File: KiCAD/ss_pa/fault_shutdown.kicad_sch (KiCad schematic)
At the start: 39 parts, among them J31 8P8C_Shielded, J5 Screw_Terminal_01x02, U1 LM393, U2 CD74HC4066, U3 LM2936-5.0_TO92

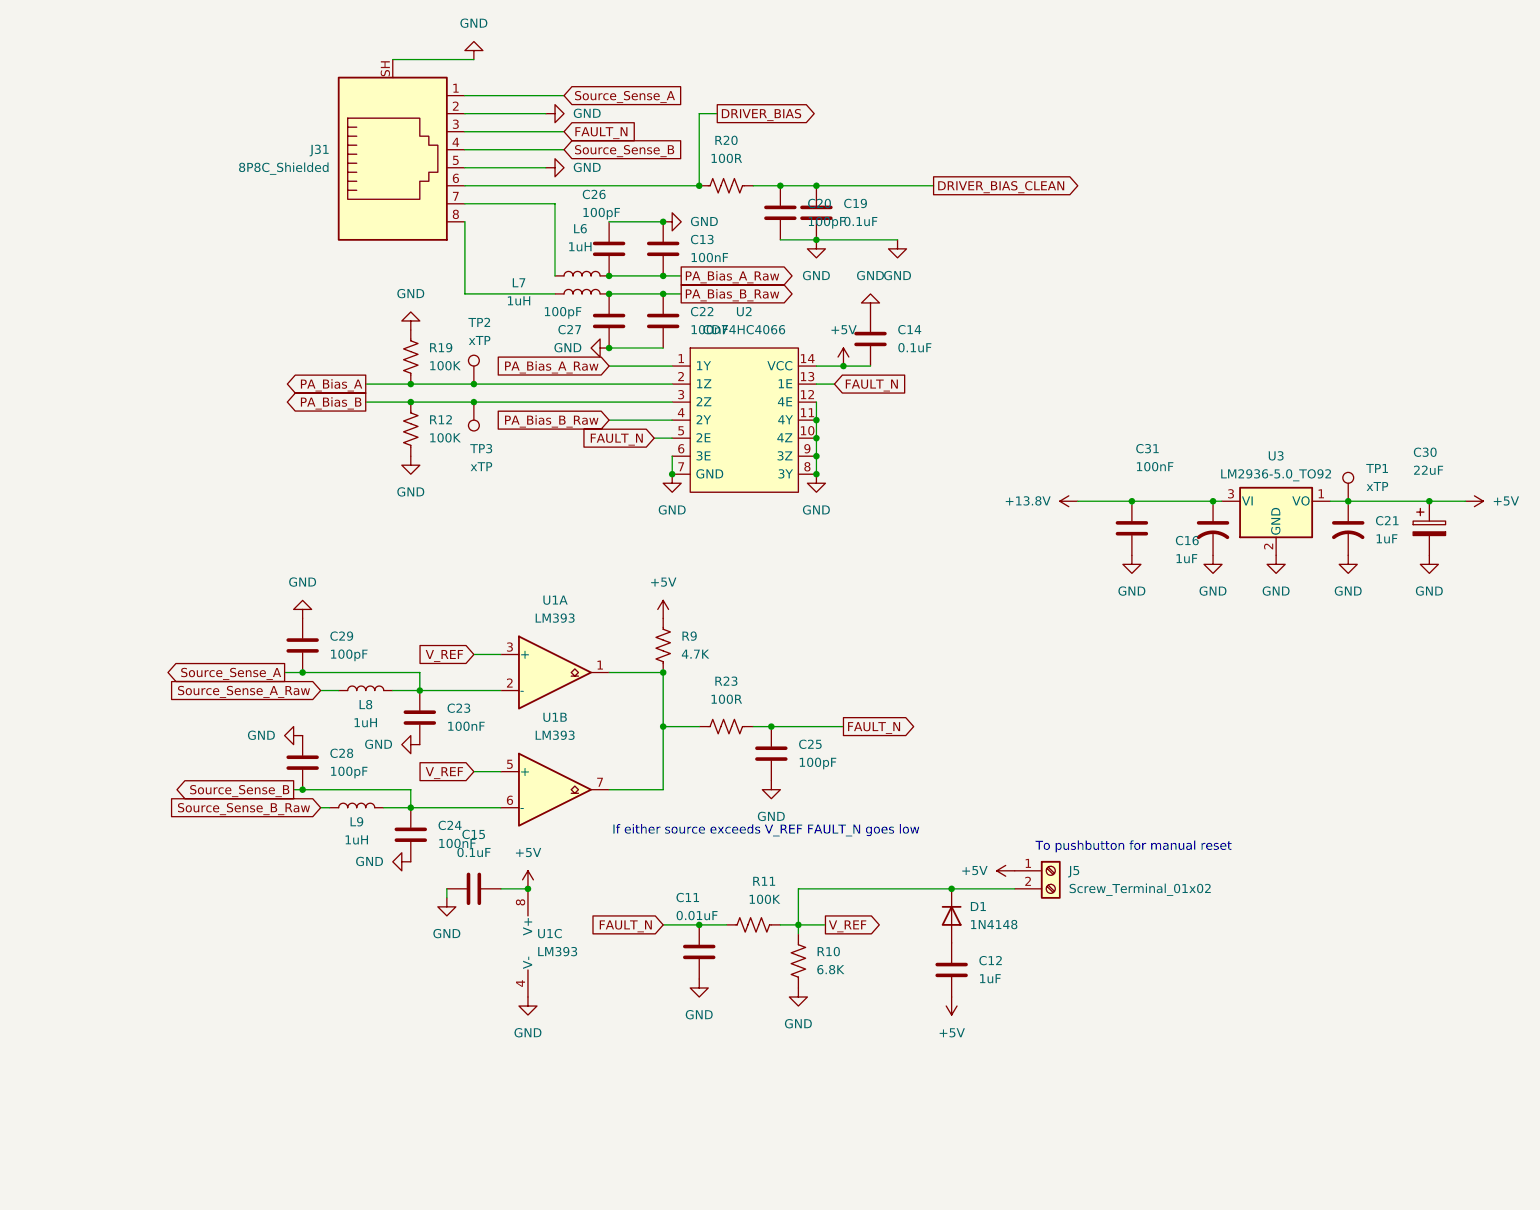
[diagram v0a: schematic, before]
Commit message: revD: ss_pa U13 LM2936 pinout fix + analog U9 74HCT125 miswiring fix
ss_pa fault_shutdown.kicad_sch: fix U13 pin-to-signal mapping so an
LM2936Z-5.0/NOPB can be installed without destruction (prior MCP1700
symbol had pin 1=GND, 2=VI, 3=VO; LM2936 datasheet is pin 1=VO, 2=GND,
3=VI).

analog dac.kicad_sch: fix U9 74HCT125 miswiring found during follow-up
audit.

Co-Authored-By: Claude Opus 4.7 <noreply@anthropic.com>
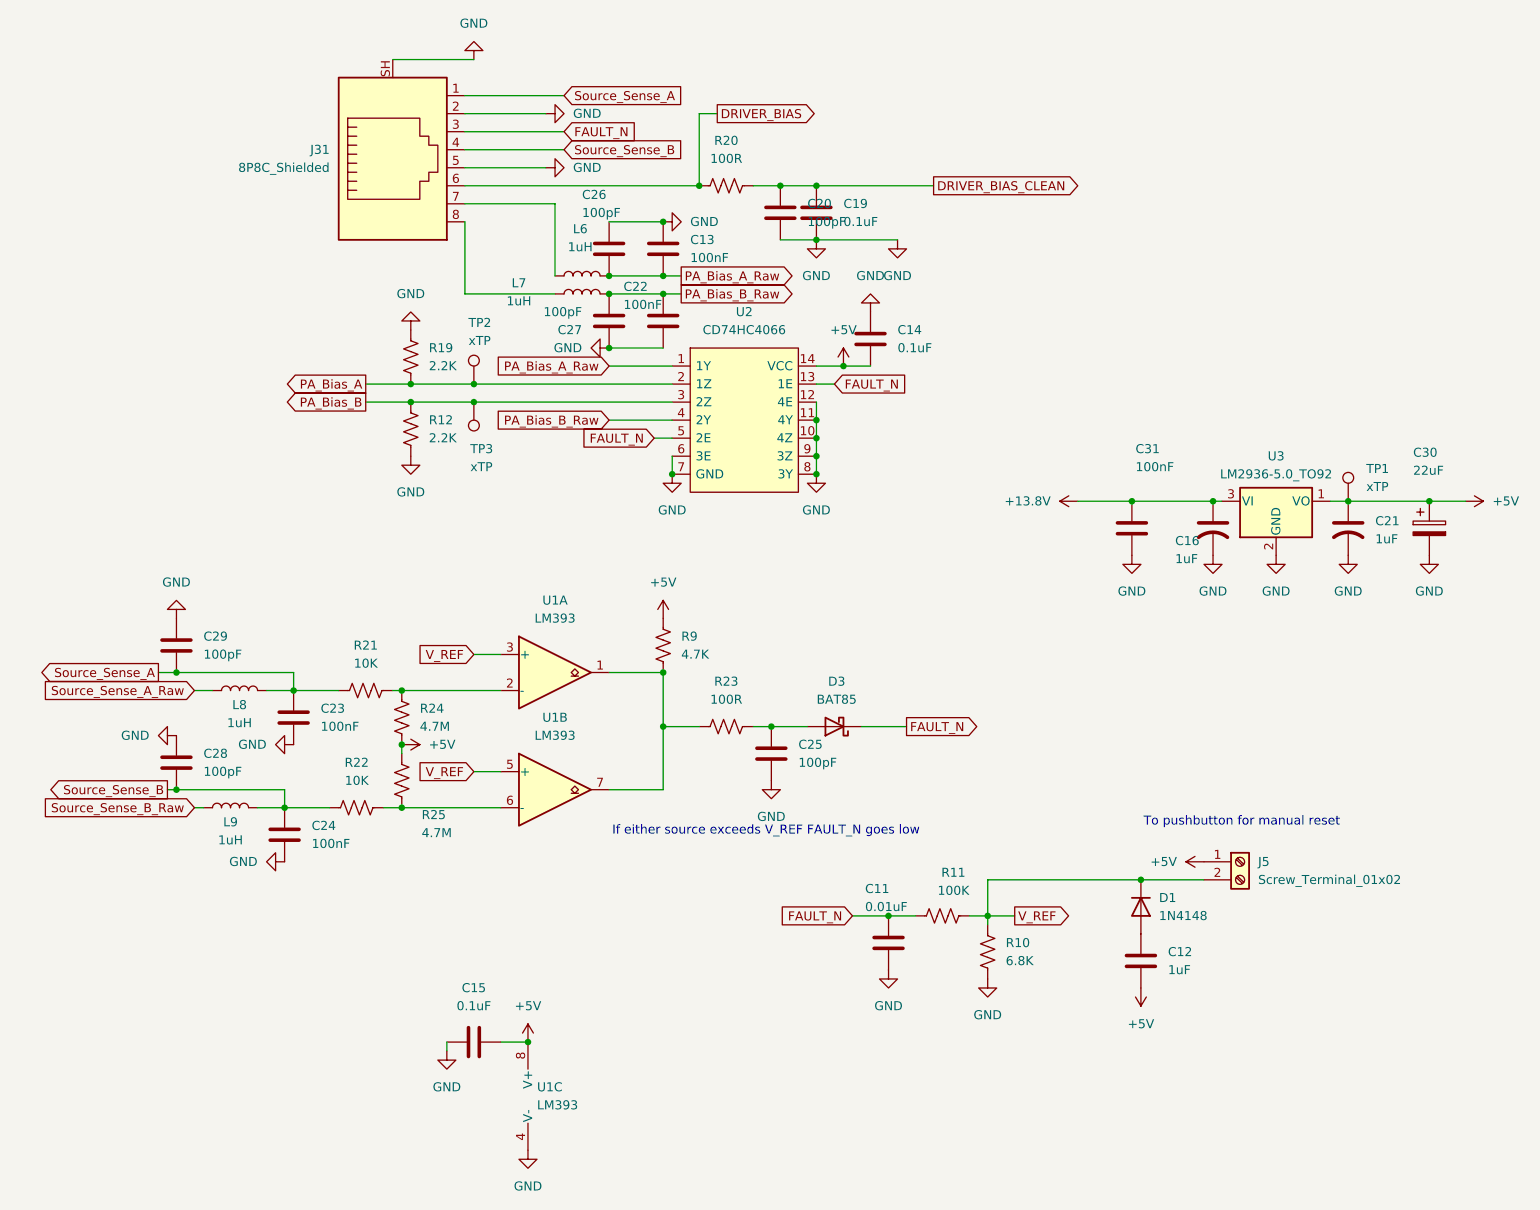
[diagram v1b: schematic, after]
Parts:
- added D3: BAT85, Diode_THT:D_DO-35_SOD27_P7.62mm_Horizontal, symbol Diode:BAT85
- added R21, R22: 10K, symbol Device:R_US
- added R24, R25: 4.7M, symbol Device:R_US
- R12, R19: value 100K -> 2.2K
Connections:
- net +5V: now also R24.2, R25.1
- net FAULT_N: now also D3.1 (K); no longer C25.1, R23.2
- net Source_Sense_A: now also R21.1; no longer U1.2 (-)
- net Source_Sense_B: now also R22.1; no longer U1.6 (-)
- new net: R22.2, R25.2, U1.6 (-)
- new net: C25.1, D3.2 (A), R23.2
- new net: R21.2, R24.1, U1.2 (-)
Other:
- moved on the sheet: C11, C12, C15, C23, C24, C28, C29, D1, J5, L8, L9, R10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

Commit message: revD: footprint pass across all boards + ss_pa fault-chain fix + LLM review brief
- New tools/assign_misc_footprints.py: lib_id-keyed footprint assigner
  (resistors, screw terminals, pin headers, LT1054); mirrors cap-script
  safe-write (UTF-8 no BOM, no CRLF translation).
- tools/assign_cap_footprints.py: added 0.47uF -> C_Rect_L7.0mm case.
- Ran both scripts across analog, ss_pa, Output LPF, frontpanel,
  protoshield, and shelved power board. ~100 fills; details in diffs.
- ss_pa: R1-R4 (0.22 ohm source sense) upgraded to 2W Yageo RSF200
  with DIN0516 L15.5mm/P20.32mm footprint; Value tagged "0.22R 2W".
  R15/R16 confirmed 1/4W (DIN0207) for BS170 source degeneration.
- analog/power: R44 15R 5W horizontal, P30.48mm footprint.
- ss_pa fault chain (from external LLM review): R21/R22 raised
  10K -> 100K to restore self-latching loop gain; new R26 = 100K
  across C12 so cap discharges between power cycles (reliable reset).
  R26 footprint pending.
- Documentation/revD_llm_review_brief.md: new, comprehensive system
  description for external LLM deep-dive (function, component values,
  power dissipation, design flaws). References all five board netlists.

Co-Authored-By: Claude Opus 4.7 <noreply@anthropic.com>
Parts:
- added R26: 100K, Resistor_THT:R_Axial_DIN0207_L6.3mm_D2.5mm_P10.16mm_Horizontal, symbol Device:R_US
- C13, C22, C23, C24, C31: footprint (none) -> Capacitor_THT:C_Disc_D5.0mm_W2.5mm_P5.00mm
- C25, C26, C27, C28, C29: footprint (none) -> Capacitor_THT:C_Rect_L7.0mm_W3.5mm_P5.00mm
- C30: footprint (none) -> Capacitor_THT:CP_Radial_D5.0mm_P2.00mm
- R20, R23, R24, R25: footprint (none) -> Resistor_THT:R_Axial_DIN0207_L6.3mm_D2.5mm_P10.16mm_Horizontal
- R21, R22: value 10K -> 100K; footprint (none) -> Resistor_THT:R_Axial_DIN0207_L6.3mm_D2.5mm_P10.16mm_Horizontal
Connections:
- net +5V: now also J5.2 (Pin_2), R26.2; no longer J5.1 (Pin_1)
- net V_REF: now also J5.1 (Pin_1); no longer J5.2 (Pin_2)
- net at C12.1, D1.2 (A): now also R26.1
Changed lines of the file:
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@@
 	)
 	(junction
+		(at 198.12 157.48)
+		(diameter 0)
+		(color 0 0 0 0)
+	)
+	(junction
 		(at 152.4 52.07)
 		(diameter 0)
@@
 	)
 	(junction
+		(at 198.12 149.86)
+		(diameter 0)
+		(color 0 0 0 0)
+	)
+	(junction
 		(at 95.25 72.39)
 		(diameter 0)
@@
 	(wire
 		(pts
+			(xy 208.28 157.48) (xy 198.12 157.48)
+		)
+		(stroke
+			(width 0)
+			(type default)
+		)
+	)
+	(wire
+		(pts
 			(xy 73.66 132.08) (xy 77.47 132.08)
 		)
@@
 	(wire
 		(pts
+			(xy 208.28 149.86) (xy 198.12 149.86)
+		)
+		(stroke
+			(width 0)
+			(type default)
+		)
+	)
+	(wire
+		(pts
 			(xy 88.9 72.39) (xy 95.25 72.39)
 		)
@@
 			)
 		)
-		(property "Footprint" ""
+		(property "Footprint" "Capacitor_THT:C_Disc_D5.0mm_W2.5mm_P5.00mm"
 			(at 79.7052 123.19 0)
 			(hide yes)
@@
 			)
 		)
-		(property "Footprint" ""
+		(property "Footprint" "Capacitor_THT:C_Disc_D5.0mm_W2.5mm_P5.00mm"
 			(at 78.4352 139.7 0)
 			(hide yes)
@@
 			)
 		)
-		(property "Footprint" ""
+		(property "Footprint" "Capacitor_THT:C_Rect_L7.0mm_W3.5mm_P5.00mm"
 			(at 124.1552 57.15 0)
 			(hide yes)
@@
 			)
 		)
-		(property "Footprint" ""
+		(property "Footprint" "Capacitor_THT:C_Rect_L7.0mm_W3.5mm_P5.00mm"
 			(at 122.2248 59.69 0)
 			(hide yes)
@@
 			)
 		)
-		(property "Footprint" ""
+		(property "Footprint" "Capacitor_THT:C_Rect_L7.0mm_W3.5mm_P5.00mm"
 			(at 63.1952 129.54 0)
 			(hide yes)
@@
 			)
 		)
-		(property "Footprint" ""
+		(property "Footprint" "Capacitor_THT:C_Disc_D5.0mm_W2.5mm_P5.00mm"
 			(at 197.8152 96.52 0)
 			(hide yes)
@@
 	)
 	(symbol
+		(lib_id "Connector:Screw_Terminal_01x02")
+		(at 212.09 142.24 0)
+		(mirror x)
+		(unit 1)
+		(body_style 1)
+		(exclude_from_sim no)
+		(in_bom yes)
+		(on_board yes)
+		(in_pos_files yes)
+		(dnp no)
+		(property "Reference" "J5"
+			(at 214.63 142.2401 0)
+			(show_name no)
+			(do_not_autoplace no)
+			(effects
+				(font
+					(size 1.27 1.27)
+				)
+				(justify left)
+			)
+		)
+		(property "Value" "Screw_Terminal_01x02"
+			(at 214.63 139.7001 0)
+			(show_name no)
+			(do_not_autoplace no)
+			(effects
+				(font
+					(size 1.27 1.27)
+				)
+				(justify left)
+			)
+		)
+		(property "Footprint" "TerminalBlock_Phoenix:TerminalBlock_Phoenix_MKDS-1,5-2_1x02_P5.00mm_Horizontal"
+			(at 212.09 142.24 0)
+			(hide yes)
+			(show_name no)
+			(do_not_autoplace no)
+			(effects
+				(font
+					(size 1.27 1.27)
+				)
+			)
+		)
+		(property "Datasheet" ""
+			(at 212.09 142.24 0)
+			(hide yes)
+			(show_name no)
+			(do_not_autoplace no)
+			(effects
+				(font
+					(size 1.27 1.27)
+				)
+			)
+		)
+		(property "Description" "Generic screw terminal, single row, 01x02, script generated (kicad-library-utils/schlib/autogen/connector/)"
+			(at 212.09 142.24 0)
+			(hide yes)
+			(show_name no)
+			(do_not_autoplace no)
+			(effects
+				(font
+					(size 1.27 1.27)
+				)
+			)
+		)
+		(pin "1"
+		)
+		(pin "2"
+		)
+		(instances
+			(project "ss_pa"
+				(path "/7b9fe991-54d6-43c4-a637-0ed9ee982c42/7e6e5903-d9c4-4499-a3fb-6a30c021fada"
+					(reference "J5")
+					(unit 1)
+				)
+			)
+		)
+	)
+	(symbol
 		(lib_id "Device:C")
 		(at 104.14 165.1 90)
@@
 			)
 		)
-		(property "Footprint" ""
+		(property "Footprint" "Capacitor_THT:C_Rect_L7.0mm_W3.5mm_P5.00mm"
 			(at 147.0152 128.27 0)
 			(hide yes)
@@
 			)
 		)
-		(property "Footprint" ""
+		(property "Footprint" "Capacitor_THT:C_Disc_D5.0mm_W2.5mm_P5.00mm"
 			(at 131.7752 57.15 0)
 			(hide yes)
@@
 			)
 		)
-		(property "Value" "10K"
+		(property "Value" "100K"
 			(at 88.9 111.76 90)
 			(show_name no)
@@
 			)
 		)
-		(property "Footprint" ""
+		(property "Footprint" "Resistor_THT:R_Axial_DIN0207_L6.3mm_D2.5mm_P10.16mm_Horizontal"
 			(at 89.154 114.554 90)
 			(hide yes)
@@
 			)
 		)
-		(property "Footprint" ""
+		(property "Footprint" "Capacitor_THT:C_Disc_D5.0mm_W2.5mm_P5.00mm"
 			(at 131.7752 67.31 0)
 			(hide yes)
@@
 	)
 	(symbol
-		(lib_id "Connector:Screw_Terminal_01x02")
-		(at 212.09 139.7 0)
-		(unit 1)
-		(body_style 1)
-		(exclude_from_sim no)
-		(in_bom yes)
-		(on_board yes)
-		(in_pos_files yes)
-		(dnp no)
-		(fields_autoplaced yes)
-		(property "Reference" "J5"
-			(at 214.63 139.6999 0)
-			(show_name no)
-			(do_not_autoplace no)
-			(effects
-				(font
-					(size 1.27 1.27)
-				)
-				(justify left)
-			)
-		)
-		(property "Value" "Screw_Terminal_01x02"
-			(at 214.63 142.2399 0)
-			(show_name no)
-			(do_not_autoplace no)
-			(effects
-				(font
-					(size 1.27 1.27)
-				)
-				(justify left)
-			)
-		)
-		(property "Footprint" "TerminalBlock_Phoenix:TerminalBlock_Phoenix_MKDS-1,5-2_1x02_P5.00mm_Horizontal"
-			(at 212.09 139.7 0)
-			(hide yes)
-			(show_name no)
-			(do_not_autoplace no)
-			(effects
-				(font
-					(size 1.27 1.27)
-				)
-			)
-		)
-		(property "Datasheet" ""
-			(at 212.09 139.7 0)
-			(hide yes)
-			(show_name no)
-			(do_not_autoplace no)
-			(effects
-				(font
-					(size 1.27 1.27)
-				)
-			)
-		)
-		(property "Description" "Generic screw terminal, single row, 01x02, script generated (kicad-library-utils/schlib/autogen/connector/)"
-			(at 212.09 139.7 0)
-			(hide yes)
-			(show_name no)
-			(do_not_autoplace no)
-			(effects
-				(font
-					(size 1.27 1.27)
-				)
-			)
-		)
-		(pin "1"
-		)
-		(pin "2"
-		)
-		(instances
-			(project "ss_pa"
-				(path "/7b9fe991-54d6-43c4-a637-0ed9ee982c42/7e6e5903-d9c4-4499-a3fb-6a30c021fada"
-					(reference "J5")
-					(unit 1)
-				)
-			)
-		)
-	)
-	(symbol
 		(lib_id "Device:R_US")
 		(at 170.18 147.32 90)
@@
 			)
 		)
-		(property "Footprint" ""
+		(property "Footprint" "Capacitor_THT:CP_Radial_D5.0mm_P2.00mm"
 			(at 239.7252 96.52 0)
 			(hide yes)
@@
 			)
 		)
-		(property "Value" "10K"
+		(property "Value" "100K"
 			(at 87.63 128.27 90)
 			(show_name no)
@@
 			)
 		)
-		(property "Footprint" ""
+		(property "Footprint" "Resistor_THT:R_Axial_DIN0207_L6.3mm_D2.5mm_P10.16mm_Horizontal"
 			(at 87.884 131.064 90)
 			(hide yes)
@@
 	)
 	(symbol
+		(lib_id "Device:R_US")
+		(at 208.28 153.67 0)
+		(unit 1)
+		(body_style 1)
+		(exclude_from_sim no)
+		(in_bom yes)
+		(on_board yes)
+		(in_pos_files yes)
+		(dnp no)
+		(fields_autoplaced yes)
+		(property "Reference" "R26"
+			(at 210.82 152.3999 0)
+			(show_name no)
+			(do_not_autoplace no)
+			(effects
+				(font
+					(size 1.27 1.27)
+				)
+				(justify left)
+			)
+		)
+		(property "Value" "100K"
+			(at 210.82 154.9399 0)
+			(show_name no)
+			(do_not_autoplace no)
+			(effects
+				(font
+					(size 1.27 1.27)
+				)
+				(justify left)
+			)
+		)
+		(property "Footprint" "Resistor_THT:R_Axial_DIN0207_L6.3mm_D2.5mm_P10.16mm_Horizontal"
+			(at 209.296 153.924 90)
+			(hide yes)
+			(show_name no)
+			(do_not_autoplace no)
+			(effects
+				(font
+					(size 1.27 1.27)
+				)
+			)
+		)
+		(property "Datasheet" ""
+			(at 208.28 153.67 0)
+			(hide yes)
+			(show_name no)
+			(do_not_autoplace no)
+			(effects
+				(font
+					(size 1.27 1.27)
+				)
+			)
+		)
+		(property "Description" "Resistor, US symbol"
+			(at 208.28 153.67 0)
+			(hide yes)
+			(show_name no)
+			(do_not_autoplace no)
+			(effects
+				(font
+					(size 1.27 1.27)
+				)
+			)
+		)
+		(pin "2"
+		)
+		(pin "1"
+		)
+		(instances
+			(project "ss_pa"
+				(path "/7b9fe991-54d6-43c4-a637-0ed9ee982c42/7e6e5903-d9c4-4499-a3fb-6a30c021fada"
+					(reference "R26")
+					(unit 1)
+				)
+			)
+		)
+	)
+	(symbol
 		(lib_id "power:GND")
 		(at 162.56 154.94 0)
@@
 			)
 		)
-		(property "Footprint" ""
+		(property "Footprint" "Resistor_THT:R_Axial_DIN0207_L6.3mm_D2.5mm_P10.16mm_Horizontal"
 			(at 94.996 128.524 90)
 			(hide yes)
@@
 			)
 		)
-		(property "Footprint" ""
+		(property "Footprint" "Capacitor_THT:C_Rect_L7.0mm_W3.5mm_P5.00mm"
 			(at 63.1952 113.03 0)
 			(hide yes)
@@
 			)
 		)
-		(property "Footprint" ""
+		(property "Footprint" "Resistor_THT:R_Axial_DIN0207_L6.3mm_D2.5mm_P10.16mm_Horizontal"
 			(at 94.996 119.634 90)
 			(hide yes)
@@
 			)
 		)
-		(property "Footprint" ""
+		(property "Footprint" "Resistor_THT:R_Axial_DIN0207_L6.3mm_D2.5mm_P10.16mm_Horizontal"
 			(at 139.954 119.634 90)
 			(hide yes)
@@
 			)
 		)
-		(property "Footprint" ""
+		(property "Footprint" "Resistor_THT:R_Axial_DIN0207_L6.3mm_D2.5mm_P10.16mm_Horizontal"
 			(at 139.954 43.434 90)
 			(hide yes)
